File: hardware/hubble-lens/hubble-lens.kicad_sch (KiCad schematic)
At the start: 43 parts, among them J101 Left, J102 Bottom, J103 Right, J201 Power

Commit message: hardware: add hubble notes
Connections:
- net +12V: now also J101.7 (Pin_7); no longer J101.3 (Pin_3), J101.5 (Pin_5)
- net -12V: now also J101.8 (Pin_8); no longer J101.4 (Pin_4), J101.6 (Pin_6)
- net GND: now also J102.4 (Pin_4), J201.3 (GND), J201.4 (GND), J201.5 (GND), J201.6 (GND), J201.7 (GND), J201.8 (GND)
- net IO22: now reaches J101.15 (Pin_15)
- net IO23: now reaches J101.16 (Pin_16)
- net IO20: now reaches J101.17 (Pin_17)
- net IO21: now reaches J101.18 (Pin_18)
- net IO14: now reaches J102.10 (Pin_10)
- net IO11: now reaches J102.13 (Pin_13)
- net IO12: now reaches J102.14 (Pin_14)
- net IO9: now reaches J102.15 (Pin_15)
- net IO10: now reaches J102.16 (Pin_16)
- net IO7: now reaches J102.21 (Pin_21)
- net IO8: now reaches J102.22 (Pin_22)
- net SER4.1: now reaches J102.23 (Pin_23)
- net SER4.0: now reaches J102.24 (Pin_24)
- net SER4.3: now reaches J102.25 (Pin_25)
- net SER4.2: now reaches J102.26 (Pin_26)
- net IO6: now reaches J102.27 (Pin_27)
- net IO19: now reaches J102.3 (Pin_3)
- net IO17: now reaches J102.5 (Pin_5)
- net IO18: now reaches J102.6 (Pin_6)
- net IO15: now reaches J102.7 (Pin_7)
- net IO16: now reaches J102.8 (Pin_8)
- net IO13: now reaches J102.9 (Pin_9)
- net SER1.3: now reaches J103.25 (Pin_25)
- net SER1.2: now reaches J103.26 (Pin_26)
- net SER1.1: now reaches J103.27 (Pin_27)
- net SER1.0: now reaches J103.28 (Pin_28)
- net -12V_SWITCHED: now reaches J201.1 (-12V), J201.2 (-12V)
- net -12V_SWITCHED: now also J101.4 (Pin_4), J101.6 (Pin_6)
- net +12V_SWITCHED: now reaches J201.10 (+12V), J201.9 (+12V)
- net +12V_SWITCHED: now also J101.3 (Pin_3), J101.5 (Pin_5)
- no-connect marks 40 -> 11
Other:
- note added: "Hubble notes: - Use switched power for the board under test. Use non-switched for components on the Lens itself. - Full scale DACs and ADCs are multiplexed. Each has 4 dedicated outputs (1-4) with 4 switched channels each (A-D). For example, DAC1 is muxed to DAC1A, 1B, 1C, and 1D. - The DAC/ADC only outputs to one switched channel at a time. Inactive channels are in Hi-Z state. - DAC/ADC outputs 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"
- moved on the sheet: J102, J103

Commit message: Rough Draft for Hubble Lens Schematic Complete
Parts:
- removed RV301, RV302, RV401, RV402, RV403, RV601, RV701: 10k, winterbloom:Potentiometer_Alpha_R0904N, symbol winterbloom:Eurorack_Pot
- added U? (x4): DG449, winterbloom:Vishay_SOT-23_8, symbol winterbloom:DG449
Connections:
- net +12V: now also U?.4 (V+), U?.4 (V+), U?.4 (V+), U?.4 (V+)
- net -12V: now also U?.7 (V-), U?.7 (V-), U?.7 (V-), U?.7 (V-)
- net ADC_1A: now also J802.T (Tip), TP201.1
- net ADC_1B: now also TP202.1
- net ADC_1C: now also TP203.1
- net DAC_1A: now also U?.8 (NO), U?.8 (NO)
- net DAC_1B: now also J402.T (Tip)
- net DAC_2A: now also J401.T (Tip)
- net DAC_2B: now also J801.T (Tip)
- net DAC_3A: now also J601.T (Tip)
- net DAC_4A: now also J701.T (Tip)
- net EXT_FG_A: now also U?.8 (NO)
- net EXT_FG_B: now also U?.8 (NO)
- net EXT_OSC_A: now also J802.TN (Tip_normalize)
- net GND: now also U?.2 (NC), U?.2 (NC), U?.3 (GND), U?.3 (GND), U?.3 (GND), U?.3 (GND)
- net IO10: now also U?.6 (IN)
- net IO11: now also U?.6 (IN)
- net LP_IN: now reaches J301.T (Tip)
- net LP_IN: now also U?.1 (COM)
- net HP_IN: now reaches J302.T (Tip)
- net HP_IN: now also U?.1 (COM)
- net IO12 renamed HP_IN_SWITCH_1
- net HP_IN_SWITCH_1: now also U?.6 (IN)
- net IO13 renamed HP_IN_SWITCH_2
- net HP_IN_SWITCH_2: now also U?.6 (IN)
- net IO2 renamed HP_VOL_SWITCH
- net IO3 renamed CUTOFF_SWITCH_1
- net IO4 renamed CUTOFF_SWITCH_2
- net IO7 renamed FM1_SWITCH_1
- net IO8 renamed FM1_SWITCH_2
- net IO9 renamed FM2_SWITCH
- new net: U?.1 (COM), U?.2 (NC) (x2)
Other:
- added sheet Knob Multiplexers (Knob_Multiplexers.kicad_sch)
- note added: "CV Tests"
- note added: "FM1 full inversion (should cut off audio): LP_VOL_SWITCH: 1 HP_VOL_SWITCH: 0 CUTOFF_SWITCH_1: 1 CUTOFF_SWITCH_2: 0 RESO_SWITCH: 0 SALT_SWITCH: 0 FM1_SWITCH_1: 0 FM1_SWITCH_2: 0 FM2_SWITCH: 0 LP_IN_SWITCH_1: 0 LP_IN_SWITCH_2: 1 HP_IN_SWITCH_1: 0 HP_IN_SWITCH_2: 0 DAC2A +5v for FM1 in"
- note added: "FM1 full: LP_VOL_SWITCH: 1 HP_VOL_SWITCH: 0 CUTOFF_SWITCH_1: 0 CUTOFF_SWITCH_2: 0 RESO_SWITCH: 0 SALT_SWITCH: 0 FM1_SWITCH_1: 1 FM1_SWITCH_2: 0 FM2_SWITCH: 0 LP_IN_SWITCH_1: 0 LP_IN_SWITCH_2: 1 HP_IN_SWITCH_1: 0 HP_IN_SWITCH_2: 0 DAC2A +5v for FM1 in"
- note added: "FM2 fully open: LP_VOL_SWITCH: 1 HP_VOL_SWITCH: 0 CUTOFF_SWITCH_1: 0 CUTOFF_SWITCH_2: 0 RESO_SWITCH: 0 SALT_SWITCH: 0 FM1_SWITCH_1: 0 FM1_SWITCH_2: 1 FM2_SWITCH: 1 LP_IN_SWITCH_1: 0 LP_IN_SWITCH_2: 1 HP_IN_SWITCH_1: 0 HP_IN_SWITCH_2: 0 DAC1B +5v for FM2 in"
- note added: "High Pass Fully Closed: LP_VOL_SWITCH: 0 HP_VOL_SWITCH: 1 CUTOFF_SWITCH_1: 1 CUTOFF_SWITCH_2: 0 RESO_SWITCH: 0 SALT_SWITCH: 0 FM1_SWITCH_1: 0 FM1_SWITCH_2: 1 FM2_SWITCH: 0 LP_IN_SWITCH_1: 0 LP_IN_SWITCH_2: 0 HP_IN_SWITCH_1: 0 HP_IN_SWITCH_2: 1 All DACS disconnected"
- note added: "High Pass Fully Open: LP_VOL_SWITCH: 0 HP_VOL_SWITCH: 1 CUTOFF_SWITCH_1: 0 CUTOFF_SWITCH_2: 0 RESO_SWITCH: 0 SALT_SWITCH: 0 FM1_SWITCH_1: 0 FM1_SWITCH_2: 1 FM2_SWITCH: 0 LP_IN_SWITCH_1: 0 LP_IN_SWITCH_2: 0 HP_IN_SWITCH_1: 0 HP_IN_SWITCH_2: 1 All DACS disconnected"
- note added: "Knob Tests"
- note added: "Limitations: Cannot control Fm2 CV or Volume CV at the same time as FM1, Salt, or Resonance, or using the audio input DAC"
- note added: "Low Pass Fully Closed: LP_VOL_SWITCH: 1 HP_VOL_SWITCH: 0 CUTOFF_SWITCH_1: 0 CUTOFF_SWITCH_2: 0 RESO_SWITCH: 0 SALT_SWITCH: 0 FM1_SWITCH_1: 0 FM1_SWITCH_2: 1 FM2_SWITCH: 0 LP_IN_SWITCH_1: 0 LP_IN_SWITCH_2: 1 HP_IN_SWITCH_1: 0 HP_IN_SWITCH_2: 0 All DACS disconnected"
- note added: "Low Pass Fully Open: LP_VOL_SWITCH: 1 HP_VOL_SWITCH: 0 CUTOFF_SWITCH_1: 1 CUTOFF_SWITCH_2: 0 RESO_SWITCH: 0 SALT_SWITCH: 0 FM1_SWITCH_1: 0 FM1_SWITCH_2: 1 FM2_SWITCH: 0 LP_IN_SWITCH_1: 0 LP_IN_SWITCH_2: 1 HP_IN_SWITCH_1: 0 HP_IN_SWITCH_2: 0 All DACS disconnected"
- note added: "Null Values (All Knobs down (except FM1 which is centered), Audio Inputs Connected to Ground, CVs disconnected): LP_VOL_SWITCH: 0 HP_VOL_SWITCH: 0 CUTOFF_SWITCH_1: 0 CUTOFF_SWITCH_2: 0 RESO_SWITCH: 0 SALT_SWITCH: 0 FM1_SWITCH_1: 0 FM1_SWITCH_2: 1 FM2_SWITCH: 0 LP_IN_SWITCH_1: 0 LP_IN_SWITCH_2: 0 HP_IN_SWITCH_1: 0 HP_IN_SWITCH_2: 0 All DACS disconnected"
- note added: "Resonance Self Oscillation: LP_VOL_SWITCH: 0 HP_VOL_SWITCH: 0 CUTOFF_SWITCH_1: 0 CUTOFF_SWITCH_2: 1 RESO_SWITCH: 0 SALT_SWITCH: 0 FM1_SWITCH_1: 0 FM1_SWITCH_2: 1 FM2_SWITCH: 1 LP_IN_SWITCH_1: 0 LP_IN_SWITCH_2: 0 HP_IN_SWITCH_1: 0 HP_IN_SWITCH_2: 0 DAC3A +4.4v for RESO in to just barely start self oscillation"
- note added: "Salty Self Oscillation: LP_VOL_SWITCH: 0 HP_VOL_SWITCH: 0 CUTOFF_SWITCH_1: 0 CUTOFF_SWITCH_2: 1 RESO_SWITCH: 0 SALT_SWITCH: 0 FM1_SWITCH_1: 0 FM1_SWITCH_2: 1 FM2_SWITCH: 1 LP_IN_SWITCH_1: 0 LP_IN_SWITCH_2: 0 HP_IN_SWITCH_1: 0 HP_IN_SWITCH_2: 0 DAC3A +4.4v for RESO in to just barely start self oscillation DAC4A +5v for full salt CV"
- note added: "Salty Self Oscillation: LP_VOL_SWITCH: 0 HP_VOL_SWITCH: 0 CUTOFF_SWITCH_1: 0 CUTOFF_SWITCH_2: 1 RESO_SWITCH: 1 SALT_SWITCH: 1 FM1_SWITCH_1: 0 FM1_SWITCH_2: 1 FM2_SWITCH: 0 LP_IN_SWITCH_1: 0 LP_IN_SWITCH_2: 0 HP_IN_SWITCH_1: 0 HP_IN_SWITCH_2: 0 All DACS disconnected"
- note added: "Self Oscillation: LP_VOL_SWITCH: 0 HP_VOL_SWITCH: 0 CUTOFF_SWITCH_1: 0 CUTOFF_SWITCH_2: 1 RESO_SWITCH: 1 SALT_SWITCH: 0 FM1_SWITCH_1: 0 FM1_SWITCH_2: 1 FM2_SWITCH: 0 LP_IN_SWITCH_1: 0 LP_IN_SWITCH_2: 0 HP_IN_SWITCH_1: 0 HP_IN_SWITCH_2: 0 All DACS disconnected"
- note added: "VCA: LP_VOL_SWITCH: 1 HP_VOL_SWITCH: 0 CUTOFF_SWITCH_1: 1 CUTOFF_SWITCH_2: 0 RESO_SWITCH: 0 SALT_SWITCH: 0 FM1_SWITCH_1: 0 FM1_SWITCH_2: 1 FM2_SWITCH: 0 LP_IN_SWITCH_1: 0 LP_IN_SWITCH_2: 1 HP_IN_SWITCH_1: 0 HP_IN_SWITCH_2: 0 DAC2B +5v for VCA full volume"
- moved on the sheet: J201, J301, J302, J401, J402, J601, J701, J801, J802

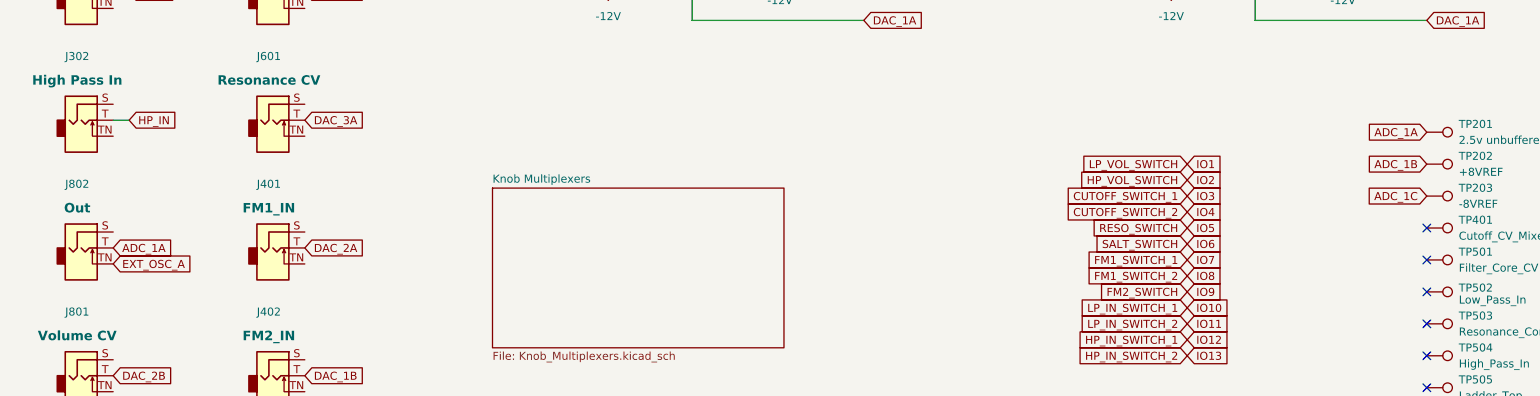
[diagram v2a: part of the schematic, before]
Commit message: Minor schematic fixes
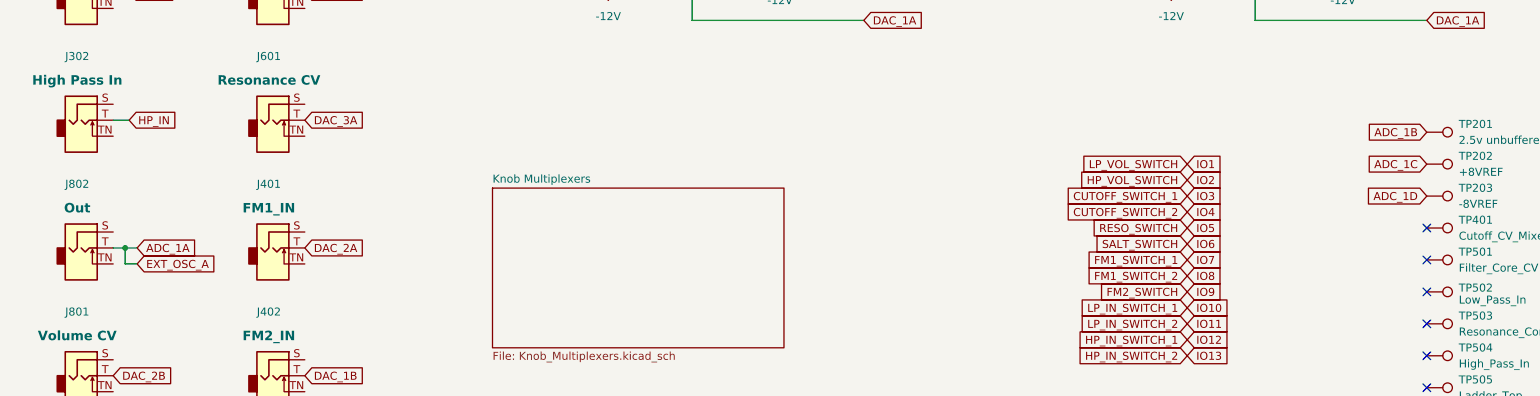
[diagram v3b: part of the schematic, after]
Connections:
- net ADC_1A: now also J103.3 (Pin_3); no longer TP201.1
- net ADC_1B: now also TP201.1; no longer TP202.1
- net ADC_1C: now also TP202.1; no longer TP203.1
- net ADC_1D: now also TP203.1
- net EXT_OSC_A: no longer names the net of J802.TN (Tip_normalize)
- net EXT_OSC_A: no longer J103.3 (Pin_3)
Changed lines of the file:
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@@
     (comment 2 "CERN-OHL-P v2")
+  )
+  (junction (at 36.83 99.695) (diameter 0) (color 0 0 0 0)
   )
   (no_connect (at 243.84 137.16))
@@
   (no_connect (at 243.84 116.84))
   (no_connect (at 243.84 127))
+  (wire (pts (xy 36.83 99.695) (xy 34.925 99.695))
+    (stroke (width 0) (type default))
+  )
   (wire (pts (xy 241.3 46.355) (xy 243.84 46.355))
     (stroke (width 0) (type default))
@@
     (stroke (width 0) (type default))
   )
+  (wire (pts (xy 38.735 99.695) (xy 36.83 99.695))
+    (stroke (width 0) (type default))
+  )
   (wire (pts (xy 127 48.895) (xy 124.46 48.895))
     (stroke (width 0) (type default))
   )
+  (wire (pts (xy 38.735 102.235) (xy 36.83 102.235))
+    (stroke (width 0) (type default))
+  )
   (wire (pts (xy 34.925 59.055) (xy 37.465 59.055))
     (stroke (width 0) (type default))
@@
   )
   (wire (pts (xy 127 38.735) (xy 130.175 38.735))
+    (stroke (width 0) (type default))
+  )
+  (wire (pts (xy 36.83 102.235) (xy 36.83 99.695))
     (stroke (width 0) (type default))
   )
@@
     )
   )
-  (global_label "ADC_1C" (shape input) (at 243.84 91.44 180) (fields_autoplaced)
-    (effects (font (size 1.27 1.27)) (justify right))
-    (property "Intersheetrefs" "${INTERSHEET_REFS}" (at 234.4333 91.44 0)
+  (global_label "ADC_1D" (shape input) (at 243.84 91.44 180) (fields_autoplaced)
+    (effects (font (size 1.27 1.27)) (justify right))
+    (property "Intersheetrefs" "${INTERSHEET_REFS}" (at 233.8585 91.44 0)
       (effects (font (size 1.27 1.27)) (justify right) hide)
     )
@@
     )
   )
-  (global_label "ADC_1B" (shape input) (at 243.84 86.36 180) (fields_autoplaced)
+  (global_label "ADC_1C" (shape input) (at 243.84 86.36 180) (fields_autoplaced)
     (effects (font (size 1.27 1.27)) (justify right))
     (property "Intersheetrefs" "${INTERSHEET_REFS}" (at 233.8585 86.36 0)
@@
     )
   )
-  (global_label "EXT_OSC_A" (shape input) (at 34.925 102.235 0) (fields_autoplaced)
-    (effects (font (size 1.27 1.27)) (justify left))
-    (property "Intersheetrefs" "${INTERSHEET_REFS}" (at 47.9907 102.235 0)
+  (global_label "EXT_OSC_A" (shape input) (at 38.735 102.235 0) (fields_autoplaced)
+    (effects (font (size 1.27 1.27)) (justify left))
+    (property "Intersheetrefs" "${INTERSHEET_REFS}" (at 51.8007 102.235 0)
       (effects (font (size 1.27 1.27)) (justify left) hide)
     )
@@
     )
   )
-  (global_label "ADC_1A" (shape input) (at 243.84 81.28 180) (fields_autoplaced)
-    (effects (font (size 1.27 1.27)) (justify right))
-    (property "Intersheetrefs" "${INTERSHEET_REFS}" (at 234.6147 81.28 0)
+  (global_label "ADC_1B" (shape input) (at 243.84 81.28 180) (fields_autoplaced)
+    (effects (font (size 1.27 1.27)) (justify right))
+    (property "Intersheetrefs" "${INTERSHEET_REFS}" (at 233.8585 81.28 0)
       (effects (font (size 1.27 1.27)) (justify right) hide)
     )
@@
     )
   )
-  (global_label "ADC_1A" (shape input) (at 34.925 99.695 0) (fields_autoplaced)
-    (effects (font (size 1.27 1.27)) (justify left))
-    (property "Intersheetrefs" "${INTERSHEET_REFS}" (at 44.7251 99.695 0)
-      (effects (font (size 1.27 1.27)) (justify left) hide)
-    )
+  (global_label "ADC_1A" (shape input) (at 38.735 99.695 0) (fields_autoplaced)
+    (effects (font (size 1.27 1.27)) (justify left))
+    (property "Intersheetrefs" "${INTERSHEET_REFS}" (at 48.5351 99.695 0)
+      (effects (font (size 1.27 1.27)) (justify left) hide)
+    )

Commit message: Rough Draft of PCB for Hubble Lens
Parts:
- added U14: DG449, winterbloom:Vishay_SOT-23_8, symbol winterbloom:DG449
- gave numbers to parts that had none: 4
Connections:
- net +12V: now also U14.4 (V+)
- net -12V: now also U14.7 (V-)
- net ADC_1B: no longer TP201.1
- net ADC_1C: no longer TP202.1
- net ADC_1D: no longer TP203.1
- net ADC_2A: now also TP201.1
- net ADC_3A: now also TP202.1
- net ADC_4A: now also TP203.1
- net DAC_2B: now also U14.8 (NO); no longer J801.T (Tip)
- net GND: now also U14.3 (GND)
- net IO14: now also U14.6 (IN)
- net at J801.TN (Tip_normalize): now also U14.2 (NC)
- new net: J801.T (Tip), U14.1 (COM)
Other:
- note added: "FM1 full inversion (should cut off audio): LP_VOL_SWITCH: 1 HP_VOL_SWITCH: 0 CUTOFF_SWITCH_1: 1 CUTOFF_SWITCH_2: 0 RESO_SWITCH: 0 SALT_SWITCH: 0 FM1_SWITCH_1: 0 FM1_SWITCH_2: 0 FM2_SWITCH: 0 LP_IN_SWITCH_1: 0 LP_IN_SWITCH_2: 1 HP_IN_SWITCH_1: 0 HP_IN_SWITCH_2: 0 VOL_JACK_SWITCH: 0 DAC2A +5v for FM1 in"
- note added: "FM1 full: LP_VOL_SWITCH: 1 HP_VOL_SWITCH: 0 CUTOFF_SWITCH_1: 0 CUTOFF_SWITCH_2: 0 RESO_SWITCH: 0 SALT_SWITCH: 0 FM1_SWITCH_1: 1 FM1_SWITCH_2: 0 FM2_SWITCH: 0 LP_IN_SWITCH_1: 0 LP_IN_SWITCH_2: 1 HP_IN_SWITCH_1: 0 HP_IN_SWITCH_2: 0 VOL_JACK_SWITCH: 0 DAC2A +5v for FM1 in"
- note added: "FM2 fully open: LP_VOL_SWITCH: 1 HP_VOL_SWITCH: 0 CUTOFF_SWITCH_1: 0 CUTOFF_SWITCH_2: 0 RESO_SWITCH: 0 SALT_SWITCH: 0 FM1_SWITCH_1: 0 FM1_SWITCH_2: 1 FM2_SWITCH: 1 LP_IN_SWITCH_1: 0 LP_IN_SWITCH_2: 1 HP_IN_SWITCH_1: 0 HP_IN_SWITCH_2: 0 VOL_JACK_SWITCH: 0 DAC1B +5v for FM2 in"
- note added: "High Pass Fully Closed: LP_VOL_SWITCH: 0 HP_VOL_SWITCH: 1 CUTOFF_SWITCH_1: 1 CUTOFF_SWITCH_2: 0 RESO_SWITCH: 0 SALT_SWITCH: 0 FM1_SWITCH_1: 0 FM1_SWITCH_2: 1 FM2_SWITCH: 0 LP_IN_SWITCH_1: 0 LP_IN_SWITCH_2: 0 HP_IN_SWITCH_1: 0 HP_IN_SWITCH_2: 1 VOL_JACK_SWITCH: 0 All DACS disconnected"
- note added: "High Pass Fully Open: LP_VOL_SWITCH: 0 HP_VOL_SWITCH: 1 CUTOFF_SWITCH_1: 0 CUTOFF_SWITCH_2: 0 RESO_SWITCH: 0 SALT_SWITCH: 0 FM1_SWITCH_1: 0 FM1_SWITCH_2: 1 FM2_SWITCH: 0 LP_IN_SWITCH_1: 0 LP_IN_SWITCH_2: 0 HP_IN_SWITCH_1: 0 HP_IN_SWITCH_2: 1 VOL_JACK_SWITCH: 0 All DACS disconnected"
- note added: "Low Pass Fully Closed: LP_VOL_SWITCH: 1 HP_VOL_SWITCH: 0 CUTOFF_SWITCH_1: 0 CUTOFF_SWITCH_2: 0 RESO_SWITCH: 0 SALT_SWITCH: 0 FM1_SWITCH_1: 0 FM1_SWITCH_2: 1 FM2_SWITCH: 0 LP_IN_SWITCH_1: 0 LP_IN_SWITCH_2: 1 HP_IN_SWITCH_1: 0 HP_IN_SWITCH_2: 0 VOL_JACK_SWITCH: 0 All DACS disconnected"
- note added: "Low Pass Fully Open: LP_VOL_SWITCH: 1 HP_VOL_SWITCH: 0 CUTOFF_SWITCH_1: 1 CUTOFF_SWITCH_2: 0 RESO_SWITCH: 0 SALT_SWITCH: 0 FM1_SWITCH_1: 0 FM1_SWITCH_2: 1 FM2_SWITCH: 0 LP_IN_SWITCH_1: 0 LP_IN_SWITCH_2: 1 HP_IN_SWITCH_1: 0 HP_IN_SWITCH_2: 0 VOL_JACK_SWITCH: 0 All DACS disconnected"
- note added: "Null Values (All Knobs down (except FM1 which is centered), Audio Inputs Connected to Ground, CVs disconnected): LP_VOL_SWITCH: 0 HP_VOL_SWITCH: 0 CUTOFF_SWITCH_1: 0 CUTOFF_SWITCH_2: 0 RESO_SWITCH: 0 SALT_SWITCH: 0 FM1_SWITCH_1: 0 FM1_SWITCH_2: 1 FM2_SWITCH: 0 LP_IN_SWITCH_1: 0 LP_IN_SWITCH_2: 0 HP_IN_SWITCH_1: 0 HP_IN_SWITCH_2: 0 VOL_JACK_SWITCH: 0 All DACS disconnected"
- note added: "Resonance Self Oscillation: LP_VOL_SWITCH: 0 HP_VOL_SWITCH: 0 CUTOFF_SWITCH_1: 0 CUTOFF_SWITCH_2: 1 RESO_SWITCH: 0 SALT_SWITCH: 0 FM1_SWITCH_1: 0 FM1_SWITCH_2: 1 FM2_SWITCH: 1 LP_IN_SWITCH_1: 0 LP_IN_SWITCH_2: 0 HP_IN_SWITCH_1: 0 HP_IN_SWITCH_2: 0 VOL_JACK_SWITCH: 0 DAC3A +4.4v for RESO in to just barely start self oscillation"
- note added: "Salty Self Oscillation: LP_VOL_SWITCH: 0 HP_VOL_SWITCH: 0 CUTOFF_SWITCH_1: 0 CUTOFF_SWITCH_2: 1 RESO_SWITCH: 0 SALT_SWITCH: 0 FM1_SWITCH_1: 0 FM1_SWITCH_2: 1 FM2_SWITCH: 1 LP_IN_SWITCH_1: 0 LP_IN_SWITCH_2: 0 HP_IN_SWITCH_1: 0 HP_IN_SWITCH_2: 0 VOL_JACK_SWITCH: 0 DAC3A +4.4v for RESO in to just barely start self oscillation DAC4A +5v for full salt CV"
- note added: "Salty Self Oscillation: LP_VOL_SWITCH: 0 HP_VOL_SWITCH: 0 CUTOFF_SWITCH_1: 0 CUTOFF_SWITCH_2: 1 RESO_SWITCH: 1 SALT_SWITCH: 1 FM1_SWITCH_1: 0 FM1_SWITCH_2: 1 FM2_SWITCH: 0 LP_IN_SWITCH_1: 0 LP_IN_SWITCH_2: 0 HP_IN_SWITCH_1: 0 HP_IN_SWITCH_2: 0 VOL_JACK_SWITCH: 0 All DACS disconnected"
- note added: "Self Oscillation: LP_VOL_SWITCH: 0 HP_VOL_SWITCH: 0 CUTOFF_SWITCH_1: 0 CUTOFF_SWITCH_2: 1 RESO_SWITCH: 1 SALT_SWITCH: 0 FM1_SWITCH_1: 0 FM1_SWITCH_2: 1 FM2_SWITCH: 0 LP_IN_SWITCH_1: 0 LP_IN_SWITCH_2: 0 HP_IN_SWITCH_1: 0 HP_IN_SWITCH_2: 0 VOL_JACK_SWITCH: 0 All DACS disconnected"
- note added: "VCA: LP_VOL_SWITCH: 1 HP_VOL_SWITCH: 0 CUTOFF_SWITCH_1: 1 CUTOFF_SWITCH_2: 0 RESO_SWITCH: 0 SALT_SWITCH: 0 FM1_SWITCH_1: 0 FM1_SWITCH_2: 1 FM2_SWITCH: 0 LP_IN_SWITCH_1: 0 LP_IN_SWITCH_2: 1 HP_IN_SWITCH_1: 0 HP_IN_SWITCH_2: 0 VOL_JACK_SWITCH: 1 DAC2B +5v for VCA full volume"
- note removed: "FM1 full inversion (should cut off audio): LP_VOL_SWITCH: 1 HP_VOL_SWITCH: 0 CUTOFF_SWITCH_1: 1 CUTOFF_SWITCH_2: 0 RESO_SWITCH: 0 SALT_SWITCH: 0 FM1_SWITCH_1: 0 FM1_SWITCH_2: 0 FM2_SWITCH: 0 LP_IN_SWITCH_1: 0 LP_IN_SWITCH_2: 1 HP_IN_SWITCH_1: 0 HP_IN_SWITCH_2: 0 DAC2A +5v for FM1 in"
- note removed: "FM1 full: LP_VOL_SWITCH: 1 HP_VOL_SWITCH: 0 CUTOFF_SWITCH_1: 0 CUTOFF_SWITCH_2: 0 RESO_SWITCH: 0 SALT_SWITCH: 0 FM1_SWITCH_1: 1 FM1_SWITCH_2: 0 FM2_SWITCH: 0 LP_IN_SWITCH_1: 0 LP_IN_SWITCH_2: 1 HP_IN_SWITCH_1: 0 HP_IN_SWITCH_2: 0 DAC2A +5v for FM1 in"
- note removed: "FM2 fully open: LP_VOL_SWITCH: 1 HP_VOL_SWITCH: 0 CUTOFF_SWITCH_1: 0 CUTOFF_SWITCH_2: 0 RESO_SWITCH: 0 SALT_SWITCH: 0 FM1_SWITCH_1: 0 FM1_SWITCH_2: 1 FM2_SWITCH: 1 LP_IN_SWITCH_1: 0 LP_IN_SWITCH_2: 1 HP_IN_SWITCH_1: 0 HP_IN_SWITCH_2: 0 DAC1B +5v for FM2 in"
- note removed: "High Pass Fully Closed: LP_VOL_SWITCH: 0 HP_VOL_SWITCH: 1 CUTOFF_SWITCH_1: 1 CUTOFF_SWITCH_2: 0 RESO_SWITCH: 0 SALT_SWITCH: 0 FM1_SWITCH_1: 0 FM1_SWITCH_2: 1 FM2_SWITCH: 0 LP_IN_SWITCH_1: 0 LP_IN_SWITCH_2: 0 HP_IN_SWITCH_1: 0 HP_IN_SWITCH_2: 1 All DACS disconnected"
- note removed: "High Pass Fully Open: LP_VOL_SWITCH: 0 HP_VOL_SWITCH: 1 CUTOFF_SWITCH_1: 0 CUTOFF_SWITCH_2: 0 RESO_SWITCH: 0 SALT_SWITCH: 0 FM1_SWITCH_1: 0 FM1_SWITCH_2: 1 FM2_SWITCH: 0 LP_IN_SWITCH_1: 0 LP_IN_SWITCH_2: 0 HP_IN_SWITCH_1: 0 HP_IN_SWITCH_2: 1 All DACS disconnected"
- note removed: "Low Pass Fully Closed: LP_VOL_SWITCH: 1 HP_VOL_SWITCH: 0 CUTOFF_SWITCH_1: 0 CUTOFF_SWITCH_2: 0 RESO_SWITCH: 0 SALT_SWITCH: 0 FM1_SWITCH_1: 0 FM1_SWITCH_2: 1 FM2_SWITCH: 0 LP_IN_SWITCH_1: 0 LP_IN_SWITCH_2: 1 HP_IN_SWITCH_1: 0 HP_IN_SWITCH_2: 0 All DACS disconnected"
- note removed: "Low Pass Fully Open: LP_VOL_SWITCH: 1 HP_VOL_SWITCH: 0 CUTOFF_SWITCH_1: 1 CUTOFF_SWITCH_2: 0 RESO_SWITCH: 0 SALT_SWITCH: 0 FM1_SWITCH_1: 0 FM1_SWITCH_2: 1 FM2_SWITCH: 0 LP_IN_SWITCH_1: 0 LP_IN_SWITCH_2: 1 HP_IN_SWITCH_1: 0 HP_IN_SWITCH_2: 0 All DACS disconnected"
- note removed: "Null Values (All Knobs down (except FM1 which is centered), Audio Inputs Connected to Ground, CVs disconnected): LP_VOL_SWITCH: 0 HP_VOL_SWITCH: 0 CUTOFF_SWITCH_1: 0 CUTOFF_SWITCH_2: 0 RESO_SWITCH: 0 SALT_SWITCH: 0 FM1_SWITCH_1: 0 FM1_SWITCH_2: 1 FM2_SWITCH: 0 LP_IN_SWITCH_1: 0 LP_IN_SWITCH_2: 0 HP_IN_SWITCH_1: 0 HP_IN_SWITCH_2: 0 All DACS disconnected"
- note removed: "Resonance Self Oscillation: LP_VOL_SWITCH: 0 HP_VOL_SWITCH: 0 CUTOFF_SWITCH_1: 0 CUTOFF_SWITCH_2: 1 RESO_SWITCH: 0 SALT_SWITCH: 0 FM1_SWITCH_1: 0 FM1_SWITCH_2: 1 FM2_SWITCH: 1 LP_IN_SWITCH_1: 0 LP_IN_SWITCH_2: 0 HP_IN_SWITCH_1: 0 HP_IN_SWITCH_2: 0 DAC3A +4.4v for RESO in to just barely start self oscillation"
- note removed: "Salty Self Oscillation: LP_VOL_SWITCH: 0 HP_VOL_SWITCH: 0 CUTOFF_SWITCH_1: 0 CUTOFF_SWITCH_2: 1 RESO_SWITCH: 0 SALT_SWITCH: 0 FM1_SWITCH_1: 0 FM1_SWITCH_2: 1 FM2_SWITCH: 1 LP_IN_SWITCH_1: 0 LP_IN_SWITCH_2: 0 HP_IN_SWITCH_1: 0 HP_IN_SWITCH_2: 0 DAC3A +4.4v for RESO in to just barely start self oscillation DAC4A +5v for full salt CV"
- note removed: "Salty Self Oscillation: LP_VOL_SWITCH: 0 HP_VOL_SWITCH: 0 CUTOFF_SWITCH_1: 0 CUTOFF_SWITCH_2: 1 RESO_SWITCH: 1 SALT_SWITCH: 1 FM1_SWITCH_1: 0 FM1_SWITCH_2: 1 FM2_SWITCH: 0 LP_IN_SWITCH_1: 0 LP_IN_SWITCH_2: 0 HP_IN_SWITCH_1: 0 HP_IN_SWITCH_2: 0 All DACS disconnected"
- note removed: "Self Oscillation: LP_VOL_SWITCH: 0 HP_VOL_SWITCH: 0 CUTOFF_SWITCH_1: 0 CUTOFF_SWITCH_2: 1 RESO_SWITCH: 1 SALT_SWITCH: 0 FM1_SWITCH_1: 0 FM1_SWITCH_2: 1 FM2_SWITCH: 0 LP_IN_SWITCH_1: 0 LP_IN_SWITCH_2: 0 HP_IN_SWITCH_1: 0 HP_IN_SWITCH_2: 0 All DACS disconnected"
- note removed: "VCA: LP_VOL_SWITCH: 1 HP_VOL_SWITCH: 0 CUTOFF_SWITCH_1: 1 CUTOFF_SWITCH_2: 0 RESO_SWITCH: 0 SALT_SWITCH: 0 FM1_SWITCH_1: 0 FM1_SWITCH_2: 1 FM2_SWITCH: 0 LP_IN_SWITCH_1: 0 LP_IN_SWITCH_2: 1 HP_IN_SWITCH_1: 0 HP_IN_SWITCH_2: 0 DAC2B +5v for VCA full volume"
- moved on the sheet: J201, J301, J302, J401, J402, J601, J701, J801, J802
